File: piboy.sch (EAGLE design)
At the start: 75 parts, among them CN4 MicroUSB, T1 MMUN2133LT1G, U1 TPS61090RSAR, U2 MCP73871

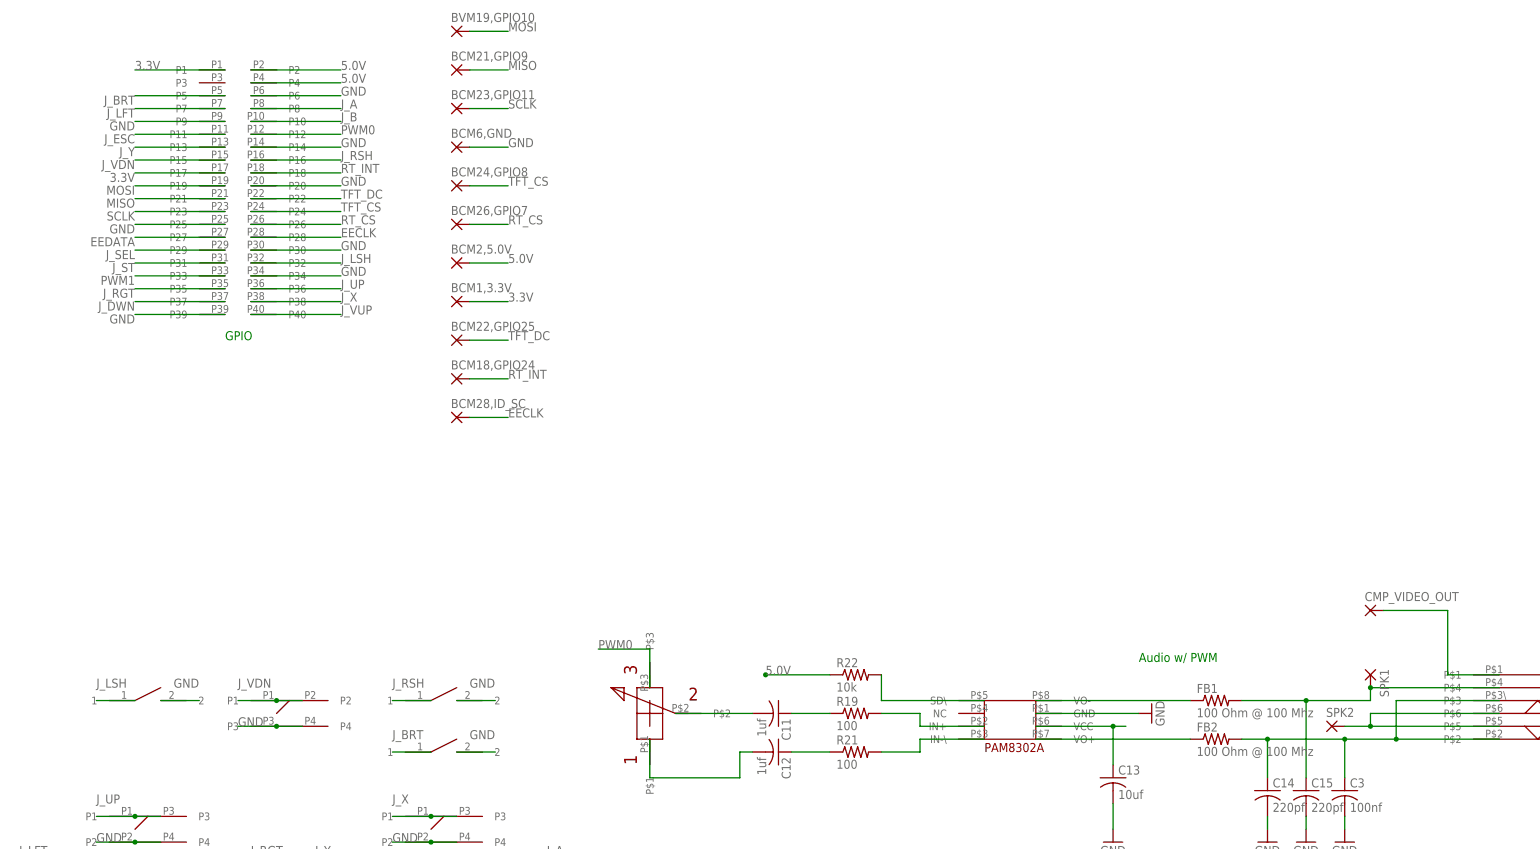
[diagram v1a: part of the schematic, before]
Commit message: -fixed problem with PAM8302 having the wrong pins -finished routing with 8mil traces and 8mil spacing -performed ground pours -finished basic silkscreen -double checked pin assignments on chips -drc passed
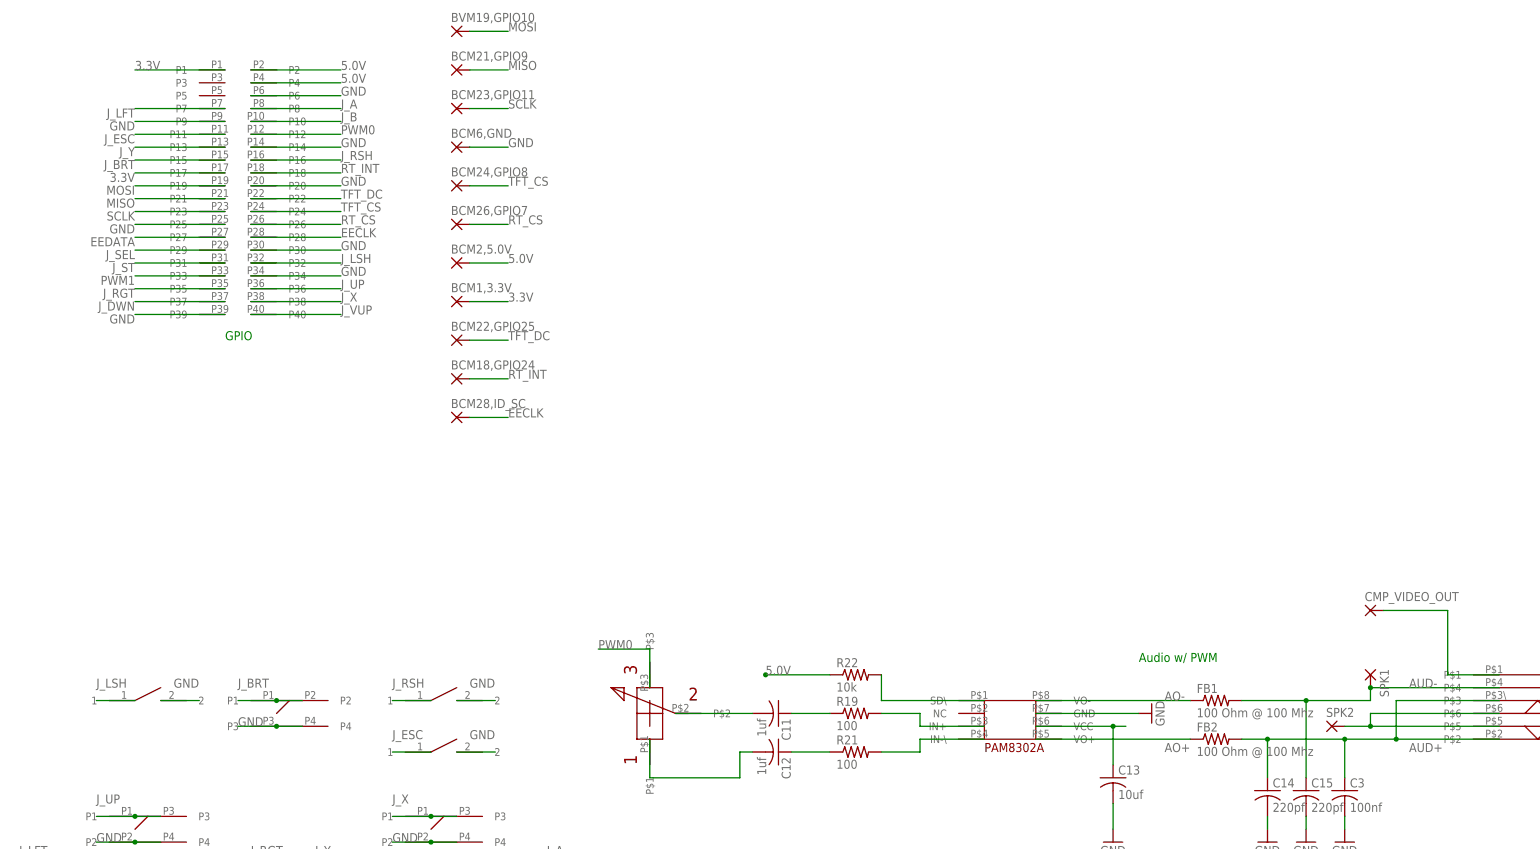
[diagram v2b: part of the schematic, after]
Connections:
- net N$18 renamed AIN-
- net N$21 renamed AIN+
- net N$22 renamed SD
- net N$23 renamed AO-
- net N$27 renamed AO+
- removed net J_VDN: U$25.P1, U$25.P2, U$9.P15
- removed net N$29: C14.1, C3.1, FB2.2, U$40.P$2, U$40.P$3
- net AUD+: now also C14.1, C3.1, FB2.2, U$40.P$2, U$40.P$3
- net J_BRT: now also U$25.P1, U$25.P2, U$9.P15; no longer U$30.1, U$9.P5
- net J_ESC: now also U$30.1

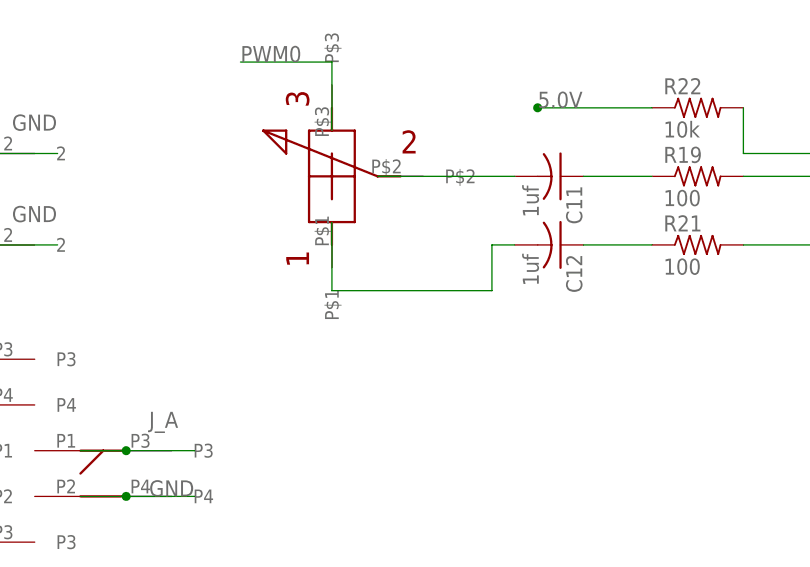
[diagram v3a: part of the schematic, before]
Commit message: -connected IN- in amp input to ground
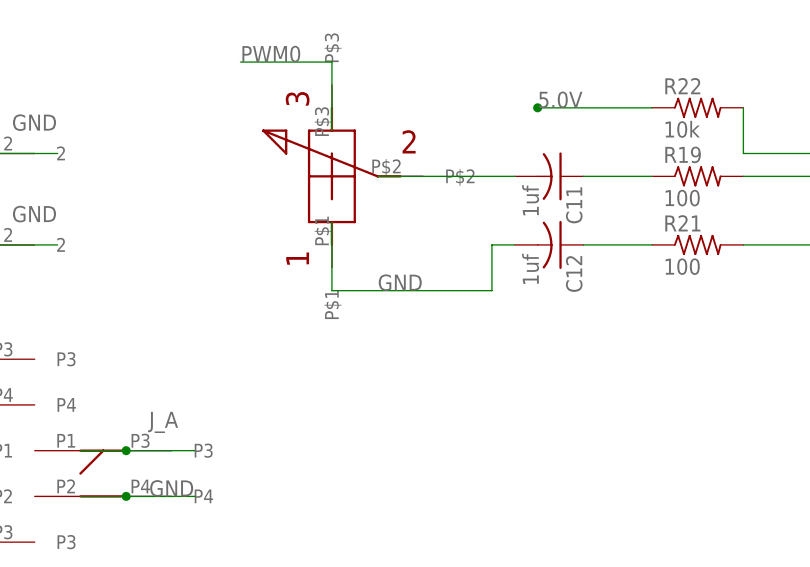
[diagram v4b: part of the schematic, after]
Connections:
- removed net N$26: C12.2, U$33.P$1
- net GND: now also C12.2, U$33.P$1
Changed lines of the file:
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@@
 <wire x1="243.84" y1="-119.38" x2="243.84" y2="-121.92" width="0.1524" layer="91"/>
+</segment>
+<segment>
+<pinref part="C12" gate="G$1" pin="2"/>
+<wire x1="127" y1="-106.68" x2="124.46" y2="-106.68" width="0.1524" layer="91"/>
+<pinref part="U$33" gate="G$1" pin="P$1"/>
+<wire x1="106.68" y1="-104.14" x2="106.68" y2="-111.76" width="0.1524" layer="91"/>
+<wire x1="106.68" y1="-111.76" x2="124.46" y2="-111.76" width="0.1524" layer="91"/>
+<wire x1="124.46" y1="-111.76" x2="124.46" y2="-106.68" width="0.1524" layer="91"/>
+<label x="111.76" y="-111.76" size="1.778" layer="95"/>
 </segment>
 </net>
@@
 </segment>
 </net>
-<net name="N$26" class="0">
-<segment>
-<pinref part="C12" gate="G$1" pin="2"/>
-<wire x1="127" y1="-106.68" x2="124.46" y2="-106.68" width="0.1524" layer="91"/>
-<pinref part="U$33" gate="G$1" pin="P$1"/>
-<wire x1="106.68" y1="-104.14" x2="106.68" y2="-111.76" width="0.1524" layer="91"/>
-<wire x1="106.68" y1="-111.76" x2="124.46" y2="-111.76" width="0.1524" layer="91"/>
-<wire x1="124.46" y1="-111.76" x2="124.46" y2="-106.68" width="0.1524" layer="91"/>
-</segment>
-</net>

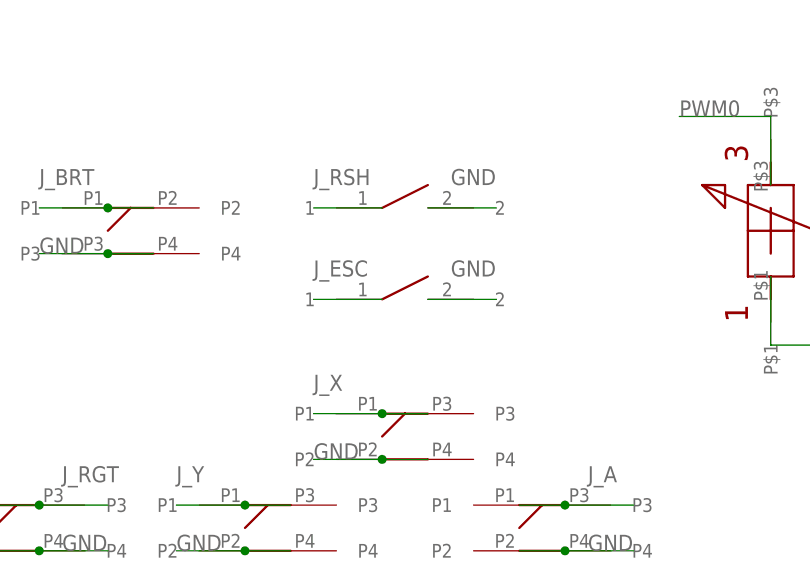
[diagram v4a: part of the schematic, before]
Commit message: -Created a new board revision 1.1 -moved layout of the screen pins -relocated the audio circuit
TODO
-Relocate the power circuit
-Fix the button smd pads
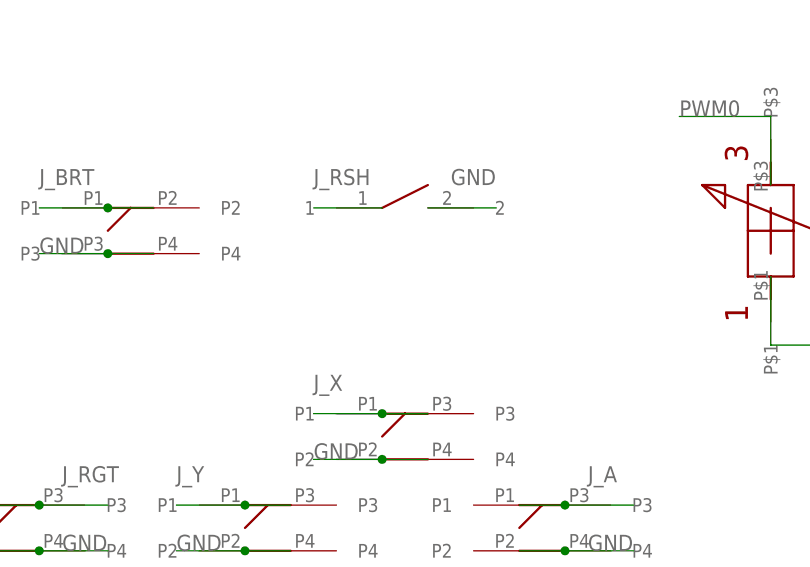
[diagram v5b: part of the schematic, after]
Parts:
- removed U$30: SWITCH_TL1105L-4,3, piboy_new:SWITCH_TL1105L-4,3
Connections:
- net GND: no longer U$30.2
- net J_ESC: no longer U$30.1
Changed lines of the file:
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@@
 <part name="U$26" library="piboy_new" deviceset="SWITCH_TL1105L-4,3" device=""/>
 <part name="U$28" library="piboy_new" deviceset="SWITCH_TL1105L-4,3" device=""/>
-<part name="U$30" library="piboy_new" deviceset="SWITCH_TL1105L-4,3" device=""/>
 <part name="BCM28,ID_SC" library="piboy_new" deviceset="WIREPAD_1,6/0,9" device=""/>
 <part name="BCM27,ID_SD" library="piboy_new" deviceset="WIREPAD_1,6/0,9" device=""/>
@@
 <instance part="U$26" gate="G$1" x="7.62" y="-96.52"/>
 <instance part="U$28" gate="G$1" x="66.04" y="-96.52"/>
-<instance part="U$30" gate="G$1" x="66.04" y="-106.68"/>
 <instance part="BCM28,ID_SC" gate="1" x="68.58" y="-40.64"/>
 <instance part="BCM27,ID_SD" gate="1" x="68.58" y="43.18"/>
@@
 </segment>
 <segment>
-<pinref part="U$30" gate="G$1" pin="2"/>
-<wire x1="68.58" y1="-106.68" x2="76.2" y2="-106.68" width="0.1524" layer="91"/>
-<label x="71.12" y="-104.14" size="1.778" layer="95"/>
-</segment>
-<segment>
 <pinref part="C13" gate="G$1" pin="2"/>
 <pinref part="GND3" gate="1" pin="GND"/>
@@
 <label x="5.08" y="15.24" size="1.778" layer="95" rot="R180"/>
 </segment>
-<segment>
-<pinref part="U$30" gate="G$1" pin="1"/>
-<wire x1="63.5" y1="-106.68" x2="55.88" y2="-106.68" width="0.1524" layer="91"/>
-<label x="55.88" y="-104.14" size="1.778" layer="95"/>
-</segment>
-</net>
+</net>

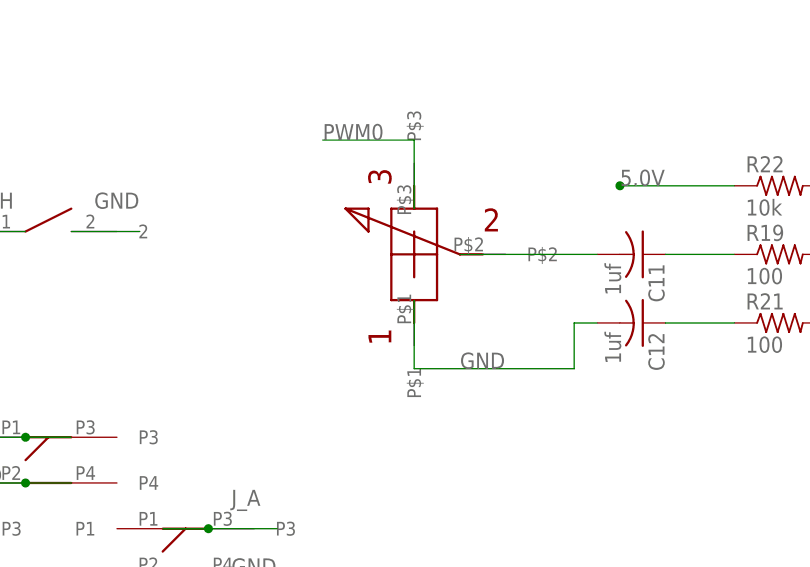
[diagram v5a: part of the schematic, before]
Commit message: -routed power circuit -routed SPI pinouts TODO -Clean up schematic: replace parts with parts that have labels, replace similar parts with all parts from the same library
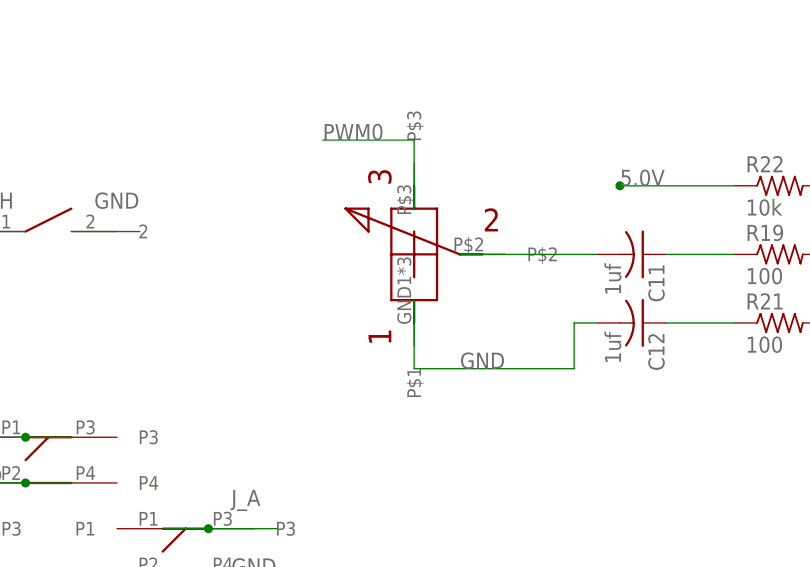
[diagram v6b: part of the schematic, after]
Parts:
- B1: device microbuilder:BATTERY -> piboy_new:MICROBUILDER_BATTERYPH2_NOTHERMALS
- U$10, U$11, U$12, U$13, U$15, U$16, U$17, U$18: value SKRRAAE010 -> PIBOY_SKRRAAE010; device piboy:SKRRAAE010 -> piboy_new:PIBOY_SKRRAAE010
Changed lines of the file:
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@@
 <part name="C1" library="adafruit" deviceset="C-US" device="C0805" value="10uF"/>
 <part name="U$4" library="microbuilder" deviceset="GND" device=""/>
-<part name="B1" library="microbuilder" deviceset="BATTERY" device="" value="JST 2-PH"/>
+<part name="B1" library="piboy_new" deviceset="MICROBUILDER_BATTERY" device="PH2_NOTHERMALS" value="JST 2-PH"/>
 <part name="U$5" library="microbuilder" deviceset="GND" device=""/>
 <part name="C2" library="adafruit" deviceset="C-US" device="C0805" value="2.2uF"/>
@@
 <part name="BCM22,GPIO25" library="piboy_new" deviceset="WIREPAD_1,6/0,9" device=""/>
 <part name="BCM18,GPIO24" library="piboy_new" deviceset="WIREPAD_1,6/0,9" device=""/>
-<part name="U$10" library="piboy" deviceset="SKRRAAE010" device=""/>
-<part name="U$11" library="piboy" deviceset="SKRRAAE010" device=""/>
-<part name="U$12" library="piboy" deviceset="SKRRAAE010" device=""/>
-<part name="U$13" library="piboy" deviceset="SKRRAAE010" device=""/>
-<part name="U$15" library="piboy" deviceset="SKRRAAE010" device=""/>
-<part name="U$16" library="piboy" deviceset="SKRRAAE010" device=""/>
-<part name="U$17" library="piboy" deviceset="SKRRAAE010" device=""/>
-<part name="U$18" library="piboy" deviceset="SKRRAAE010" device=""/>
+<part name="U$10" library="piboy_new" deviceset="PIBOY_SKRRAAE010" device=""/>
+<part name="U$11" library="piboy_new" deviceset="PIBOY_SKRRAAE010" device=""/>
+<part name="U$12" library="piboy_new" deviceset="PIBOY_SKRRAAE010" device=""/>
+<part name="U$13" library="piboy_new" deviceset="PIBOY_SKRRAAE010" device=""/>
+<part name="U$15" library="piboy_new" deviceset="PIBOY_SKRRAAE010" device=""/>
+<part name="U$16" library="piboy_new" deviceset="PIBOY_SKRRAAE010" device=""/>
+<part name="U$17" library="piboy_new" deviceset="PIBOY_SKRRAAE010" device=""/>
+<part name="U$18" library="piboy_new" deviceset="PIBOY_SKRRAAE010" device=""/>
 <part name="U$21" library="piboy" deviceset="TL3315NF100Q" device=""/>
 <part name="U$22" library="piboy" deviceset="TL3315NF100Q" device=""/>
